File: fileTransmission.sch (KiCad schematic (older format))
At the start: 25 parts, among them U14 74HCT107, U15 CD74AC161M, U16 LTC6990CS6, U17 LTC6994xS6-1, U18 74AHC1G32, U19 74AHC1G32, U20 74AHC1G08, U21 74AHC1G32, U22 74AHC1G04, U23 74AHC1G04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

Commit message: Fixing LSB first issue #1
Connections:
- net TX_REG_0: now also U26.6 (D7); no longer U26.11 (D0)
- net TX_REG_1: now also U26.5 (D6); no longer U26.12 (D1)
- net TX_REG_2: now also U26.4 (D5); no longer U26.13 (D2)
- net TX_REG_3: now also U26.3 (D4); no longer U26.14 (D3)
- net TX_REG_4: now also U26.14 (D3); no longer U26.3 (D4)
- net TX_REG_5: now also U26.13 (D2); no longer U26.4 (D5)
- net TX_REG_6: now also U26.12 (D1); no longer U26.5 (D6)
- net TX_REG_7: now also U26.11 (D0); no longer U26.6 (D7)
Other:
- note added: "LSB first"
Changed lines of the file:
@@
 Wire Wire Line
 	9100 3750 9100 3700
+Text Label 8600 4900 2    50   ~ 0
+TX_REG_0
+Text Label 8600 4800 2    50   ~ 0
+TX_REG_1
+Text Label 8600 4700 2    50   ~ 0
+TX_REG_2
+Text Label 8600 4600 2    50   ~ 0
+TX_REG_3
+Text Label 8600 4500 2    50   ~ 0
+TX_REG_4
+Text Label 8600 4400 2    50   ~ 0
+TX_REG_5
+Text Label 8600 4300 2    50   ~ 0
+TX_REG_6
 Text Label 8600 4200 2    50   ~ 0
-TX_REG_0
-Text Label 8600 4300 2    50   ~ 0
-TX_REG_1
-Text Label 8600 4400 2    50   ~ 0
-TX_REG_2
-Text Label 8600 4500 2    50   ~ 0
-TX_REG_3
-Text Label 8600 4600 2    50   ~ 0
-TX_REG_4
-Text Label 8600 4700 2    50   ~ 0
-TX_REG_5
-Text Label 8600 4800 2    50   ~ 0
-TX_REG_6
-Text Label 8600 4900 2    50   ~ 0
 TX_REG_7
 Text Label 1850 2650 0    50   ~ 0
@@
 	3250 4400 3300 4400
 Connection ~ 3250 4400
+Text Notes 8200 4000 0    50   ~ 0
+LSB first
 $EndSCHEMATC

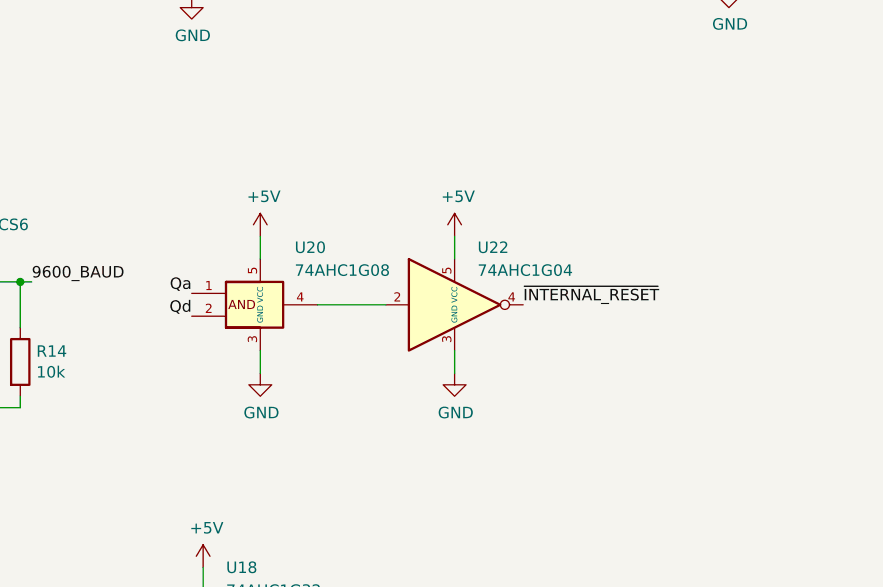
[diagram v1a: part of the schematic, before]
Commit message: Optimize gates count by replacing AND,INV with NAND
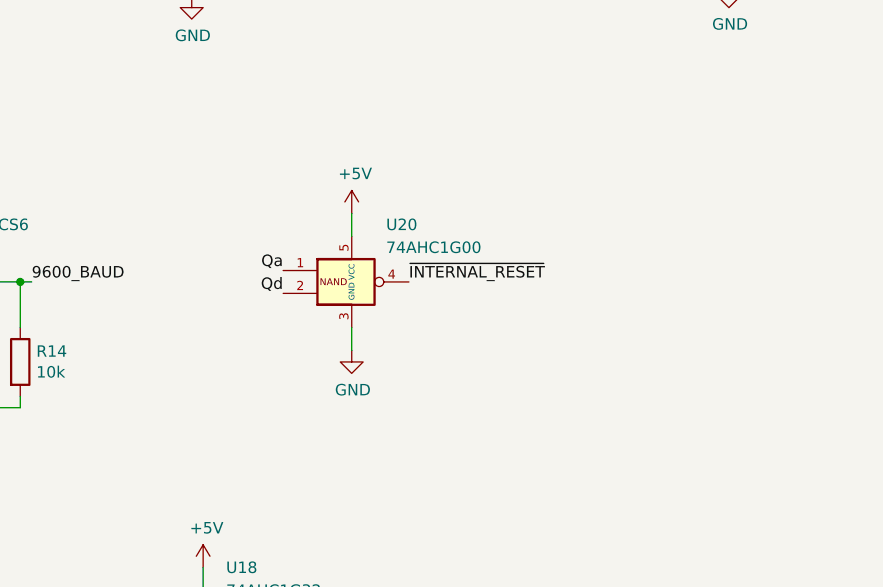
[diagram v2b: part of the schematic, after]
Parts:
- removed U20: 74AHC1G08, Package_TO_SOT_SMD:SOT-23-5, symbol Custom:74AHC1G08
- removed U22: 74AHC1G04, Package_TO_SOT_SMD:SOT-23-5, symbol Custom:74AHC1G04
- added U20: 74AHC1G00, symbol Custom:74AHC1G00
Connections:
- net +5V: now also U20.5 (VCC)
- net GND: now also U20.3 (GND)
- net Qa: now also U20.1
- net Qd: now also U20.2
- net ~INTERNAL_RESET: now also U20.4
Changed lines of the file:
@@
 	2900 2450 3600 2450
-$Comp
-L Custom:74AHC1G08 U20
-U 1 1 5FF3231F
-P 4300 4500
-F 0 "U20" H 4450 4750 50  0000 L CNN
-F 1 "74AHC1G08" H 4450 4650 50  0000 L CNN
-F 2 "Package_TO_SOT_SMD:SOT-23-5" H 4300 4500 50  0001 C CNN
-F 3 "https://assets.nexperia.com/documents/data-sheet/74AHC_AHCT1G08.pdf" H 4300 4500 50  0001 C CNN
-	1    4300 4500
-	1    0    0    -1
-$EndComp
 $Comp
 L power:GND #PWR058
 U 1 1 5FF32325
-P 4300 4800
-F 0 "#PWR058" H 4300 4550 50  0001 C CNN
-F 1 "GND" H 4305 4627 50  0000 C CNN
-F 2 "" H 4300 4800 50  0001 C CNN
-F 3 "" H 4300 4800 50  0001 C CNN
-	1    4300 4800
+P 4700 4700
+F 0 "#PWR058" H 4700 4450 50  0001 C CNN
+F 1 "GND" H 4705 4527 50  0000 C CNN
+F 2 "" H 4700 4700 50  0001 C CNN
+F 3 "" H 4700 4700 50  0001 C CNN
+	1    4700 4700
 	1    0    0    -1
 $EndComp
@@
 L power:+5V #PWR057
 U 1 1 5FF3232B
-P 4300 4200
-F 0 "#PWR057" H 4300 4050 50  0001 C CNN
-F 1 "+5V" H 4315 4373 50  0000 C CNN
-F 2 "" H 4300 4200 50  0001 C CNN
-F 3 "" H 4300 4200 50  0001 C CNN
-	1    4300 4200
-	1    0    0    -1
-$EndComp
-Wire Wire Line
-	4300 4300 4300 4200
-Wire Wire Line
-	4300 4700 4300 4800
-Text Label 4000 4450 2    50   ~ 0
+P 4700 4100
+F 0 "#PWR057" H 4700 3950 50  0001 C CNN
+F 1 "+5V" H 4715 4273 50  0000 C CNN
+F 2 "" H 4700 4100 50  0001 C CNN
+F 3 "" H 4700 4100 50  0001 C CNN
+	1    4700 4100
+	1    0    0    -1
+$EndComp
+Wire Wire Line
+	4700 4200 4700 4100
+Wire Wire Line
+	4700 4600 4700 4700
+Text Label 4400 4350 2    50   ~ 0
 Qa
-Text Label 4000 4550 2    50   ~ 0
+Text Label 4400 4450 2    50   ~ 0
 Qd
-Wire Wire Line
-	5150 4300 5150 4200
-Wire Wire Line
-	5150 4700 5150 4800
-$Comp
-L power:GND #PWR062
-U 1 1 5FF3CAFE
-P 5150 4800
-F 0 "#PWR062" H 5150 4550 50  0001 C CNN
-F 1 "GND" H 5155 4627 50  0000 C CNN
-F 2 "" H 5150 4800 50  0001 C CNN
-F 3 "" H 5150 4800 50  0001 C CNN
-	1    5150 4800
-	1    0    0    -1
-$EndComp
-$Comp
-L power:+5V #PWR061
-U 1 1 5FF3CB04
-P 5150 4200
-F 0 "#PWR061" H 5150 4050 50  0001 C CNN
-F 1 "+5V" H 5165 4373 50  0000 C CNN
-F 2 "" H 5150 4200 50  0001 C CNN
-F 3 "" H 5150 4200 50  0001 C CNN
-	1    5150 4200
-	1    0    0    -1
-$EndComp
-$Comp
-L Custom:74AHC1G04 U22
-U 1 1 5FF3CB0A
-P 5150 4500
-F 0 "U22" H 5250 4750 50  0000 L CNN
-F 1 "74AHC1G04" H 5250 4650 50  0000 L CNN
-F 2 "Package_TO_SOT_SMD:SOT-23-5" H 5150 4500 50  0001 C CNN
-F 3 "https://assets.nexperia.com/documents/data-sheet/74AHC_AHCT1G04.pdf" H 5150 4500 50  0001 C CNN
-	1    5150 4500
-	1    0    0    -1
-$EndComp
-Wire Wire Line
-	4550 4500 4850 4500
-Text Label 5450 4500 0    50   ~ 0
+Text Label 4950 4400 0    50   ~ 0
 ~INTERNAL_RESET
 Text Label 1600 6250 2    50   ~ 0
@@
 Text Notes 8200 4000 0    50   ~ 0
 LSB first
+$Comp
+L Custom:74AHC1G00 U?
+U 1 1 609F560E
+P 4700 4400
+AR Path="/609F560E" Ref="U?"  Part="1"
+AR Path="/5FE44E7A/609F560E" Ref="U20"  Part="1"
+F 0 "U20" H 4850 4650 50  0000 L CNN
+F 1 "74AHC1G00" H 4850 4550 50  0000 L CNN
+F 2 "" H 4700 4400 50  0001 C CNN
+F 3 "https://assets.nexperia.com/documents/data-sheet/74AHC_AHCT1G00.pdf" H 4700 4400 50  0001 C CNN
+	1    4700 4400
+	1    0    0    -1
+$EndComp
 $EndSCHEMATC
